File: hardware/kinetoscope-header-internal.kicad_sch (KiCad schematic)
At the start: 1 part

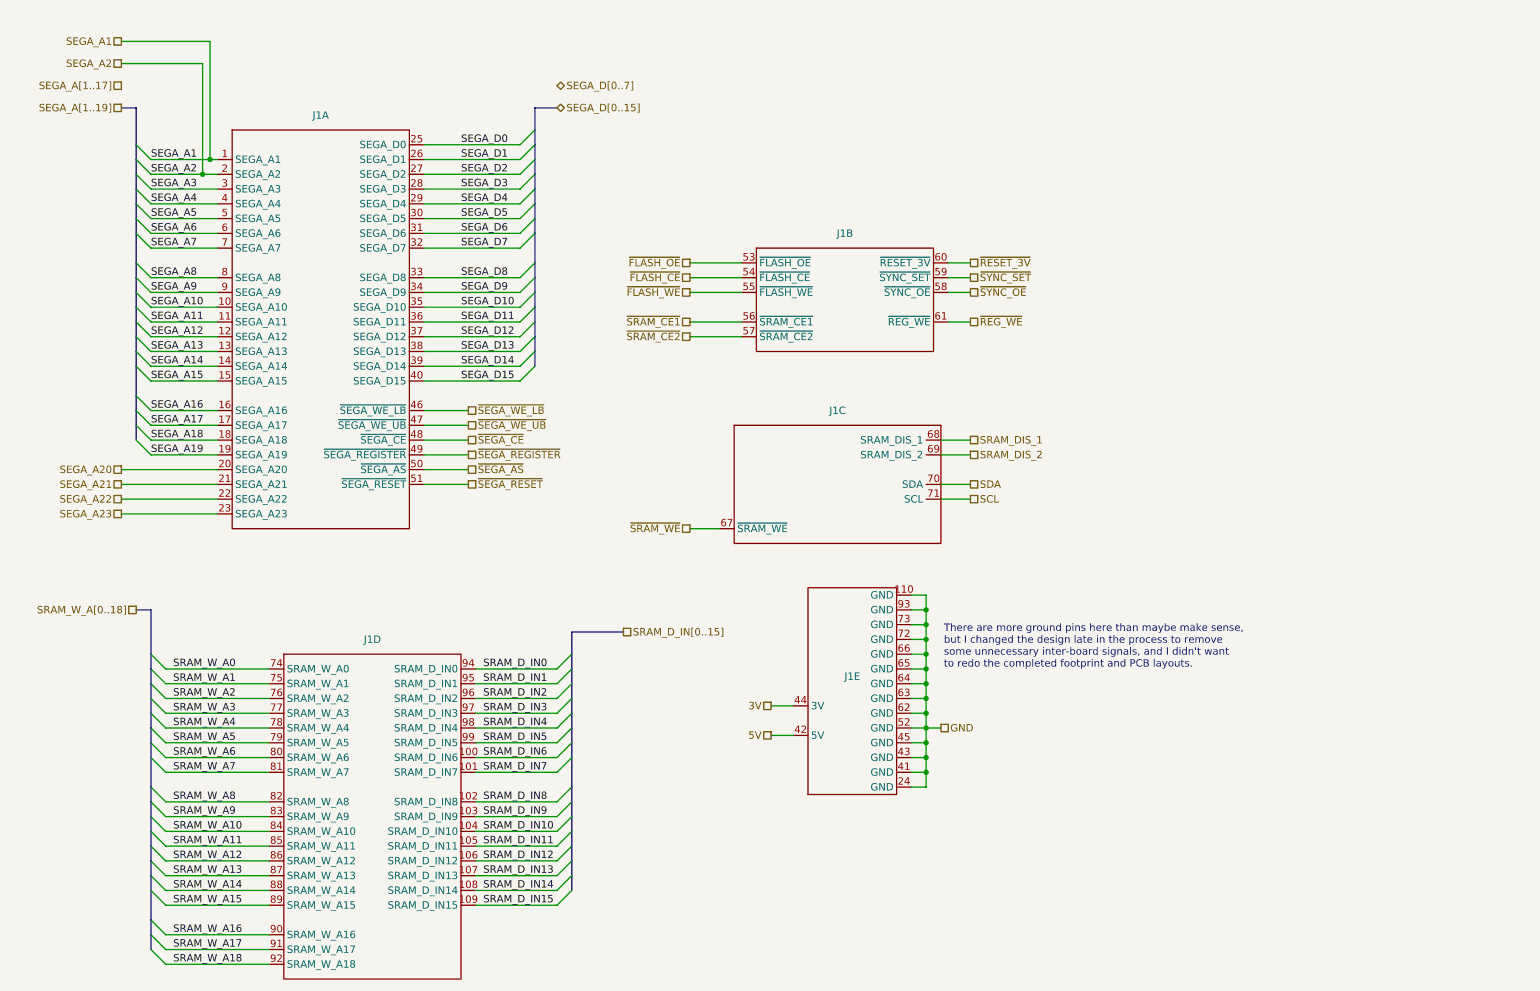
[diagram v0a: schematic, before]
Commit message: Massively reorganize board designs
Now planning to have most assembly done by JLCPCB, so trace sizes,
part selections, etc. are set accordingly.

New boards are:
 - cartridge interface & flash
 - microcontroller & registers
 - sram x2
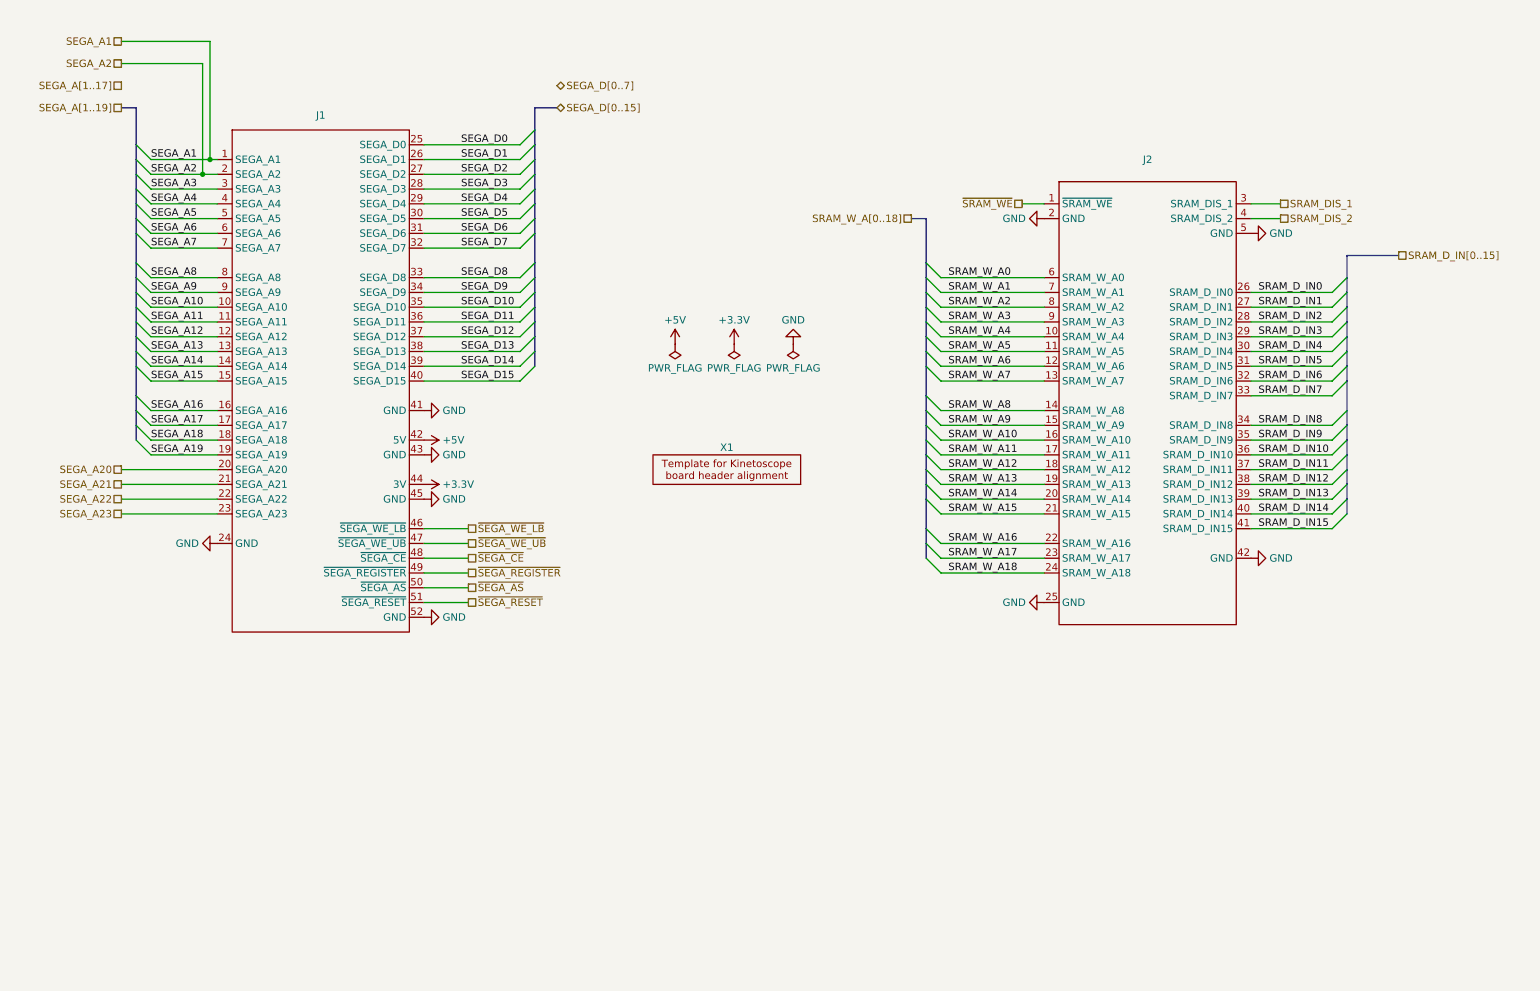
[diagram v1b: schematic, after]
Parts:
- removed J1: ~, kinetoscope-cart-header:kinetoscope-cart-header, symbol kinetoscope-cart-header:kinetoscope-cart-header
- added J1: ~, Connector_PinHeader_2.54mm:PinHeader_2x26_P2.54mm_Vertical, symbol kinetoscope-cart-header:kinetoscope-cart-header-a
- added J2: ~, Connector_PinHeader_2.54mm:PinHeader_2x21_P2.54mm_Vertical, symbol kinetoscope-cart-header:kinetoscope-cart-header-b
- added X1: ~, kinetoscope-cart-header:kinetoscope-cart-board-template, symbol kinetoscope-cart-header:kinetoscope-cart-template
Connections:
- net GND: now also J1.24 (GND), J1.41 (GND), J1.43 (GND), J1.45 (GND), J1.52 (GND), J2.2 (GND), J2.25 (GND), J2.42 (GND), J2.5 (GND)
- net SEGA_A1: now also J1.1 (SEGA_A1)
- net SEGA_A10: now also J1.10 (SEGA_A10)
- net SEGA_A11: now also J1.11 (SEGA_A11)
- net SEGA_A12: now also J1.12 (SEGA_A12)
- net SEGA_A13: now also J1.13 (SEGA_A13)
- net SEGA_A14: now also J1.14 (SEGA_A14)
- net SEGA_A15: now also J1.15 (SEGA_A15)
- net SEGA_A16: now also J1.16 (SEGA_A16)
- net SEGA_A17: now also J1.17 (SEGA_A17)
- net SEGA_A18: now also J1.18 (SEGA_A18)
- net SEGA_A19: now also J1.19 (SEGA_A19)
- net SEGA_A2: now also J1.2 (SEGA_A2)
- net SEGA_A20: now also J1.20 (SEGA_A20)
- net SEGA_A21: now also J1.21 (SEGA_A21)
- net SEGA_A22: now also J1.22 (SEGA_A22)
- net SEGA_A23: now also J1.23 (SEGA_A23)
- net SEGA_A3: now also J1.3 (SEGA_A3)
- net SEGA_A4: now also J1.4 (SEGA_A4)
- net SEGA_A5: now also J1.5 (SEGA_A5)
- net SEGA_A6: now also J1.6 (SEGA_A6)
- net SEGA_A7: now also J1.7 (SEGA_A7)
- net SEGA_A8: now also J1.8 (SEGA_A8)
- net SEGA_A9: now also J1.9 (SEGA_A9)
- net SEGA_D0: now also J1.25 (SEGA_D0)
- net SEGA_D1: now also J1.26 (SEGA_D1)
- net SEGA_D10: now also J1.35 (SEGA_D10)
- net SEGA_D11: now also J1.36 (SEGA_D11)
- net SEGA_D12: now also J1.37 (SEGA_D12)
- net SEGA_D13: now also J1.38 (SEGA_D13)
- net SEGA_D14: now also J1.39 (SEGA_D14)
- net SEGA_D15: now also J1.40 (SEGA_D15)
- net SEGA_D2: now also J1.27 (SEGA_D2)
- net SEGA_D3: now also J1.28 (SEGA_D3)
- net SEGA_D4: now also J1.29 (SEGA_D4)
- net SEGA_D5: now also J1.30 (SEGA_D5)
- net SEGA_D6: now also J1.31 (SEGA_D6)
- net SEGA_D7: now also J1.32 (SEGA_D7)
- net SEGA_D8: now also J1.33 (SEGA_D8)
- net SEGA_D9: now also J1.34 (SEGA_D9)
- net SRAM_DIS_1: now also J2.3 (SRAM_DIS_1)
- net SRAM_DIS_2: now also J2.4 (SRAM_DIS_2)
- net SRAM_D_IN0: now also J2.26 (SRAM_D_IN0)
- net SRAM_D_IN1: now also J2.27 (SRAM_D_IN1)
- net SRAM_D_IN10: now also J2.36 (SRAM_D_IN10)
- net SRAM_D_IN11: now also J2.37 (SRAM_D_IN11)
- net SRAM_D_IN12: now also J2.38 (SRAM_D_IN12)
- net SRAM_D_IN13: now also J2.39 (SRAM_D_IN13)
- net SRAM_D_IN14: now also J2.40 (SRAM_D_IN14)
- net SRAM_D_IN15: now also J2.41 (SRAM_D_IN15)
- net SRAM_D_IN2: now also J2.28 (SRAM_D_IN2)
- net SRAM_D_IN3: now also J2.29 (SRAM_D_IN3)
- net SRAM_D_IN4: now also J2.30 (SRAM_D_IN4)
- net SRAM_D_IN5: now also J2.31 (SRAM_D_IN5)
- net SRAM_D_IN6: now also J2.32 (SRAM_D_IN6)
- net SRAM_D_IN7: now also J2.33 (SRAM_D_IN7)
- net SRAM_D_IN8: now also J2.34 (SRAM_D_IN8)
- net SRAM_D_IN9: now also J2.35 (SRAM_D_IN9)
- net SRAM_W_A0: now also J2.6 (SRAM_W_A0)
- net SRAM_W_A1: now also J2.7 (SRAM_W_A1)
- net SRAM_W_A10: now also J2.16 (SRAM_W_A10)
- net SRAM_W_A11: now also J2.17 (SRAM_W_A11)
- net SRAM_W_A12: now also J2.18 (SRAM_W_A12)
- net SRAM_W_A13: now also J2.19 (SRAM_W_A13)
- net SRAM_W_A14: now also J2.20 (SRAM_W_A14)
- net SRAM_W_A15: now also J2.21 (SRAM_W_A15)
- net SRAM_W_A16: now also J2.22 (SRAM_W_A16)
- net SRAM_W_A17: now also J2.23 (SRAM_W_A17)
- net SRAM_W_A18: now also J2.24 (SRAM_W_A18)
- net SRAM_W_A2: now also J2.8 (SRAM_W_A2)
- net SRAM_W_A3: now also J2.9 (SRAM_W_A3)
- net SRAM_W_A4: now also J2.10 (SRAM_W_A4)
- net SRAM_W_A5: now also J2.11 (SRAM_W_A5)
- net SRAM_W_A6: now also J2.12 (SRAM_W_A6)
- net SRAM_W_A7: now also J2.13 (SRAM_W_A7)
- net SRAM_W_A8: now also J2.14 (SRAM_W_A8)
- net SRAM_W_A9: now also J2.15 (SRAM_W_A9)
- net ~{SEGA_AS}: now also J1.50 (~{SEGA_AS})
- net ~{SEGA_CE}: now also J1.48 (~{SEGA_CE})
- net ~{SEGA_REGISTER}: now also J1.49 (~{SEGA_REGISTER})
- net ~{SEGA_RESET}: now also J1.51 (~{SEGA_RESET})
- net ~{SEGA_WE_LB}: now also J1.46 (~{SEGA_WE_LB})
- net ~{SEGA_WE_UB}: now also J1.47 (~{SEGA_WE_UB})
- net ~{SRAM_WE}: now also J2.1 (~{SRAM_WE})
- new net +3.3V: J1.44 (3V)
- new net +5V: J1.42 (5V)
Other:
- note removed: "There are more ground pins here than maybe make sense, but I changed the design late in the process to remove some unnecessary inter-board signals, and I didn't want to redo the completed footprint and PCB layouts."

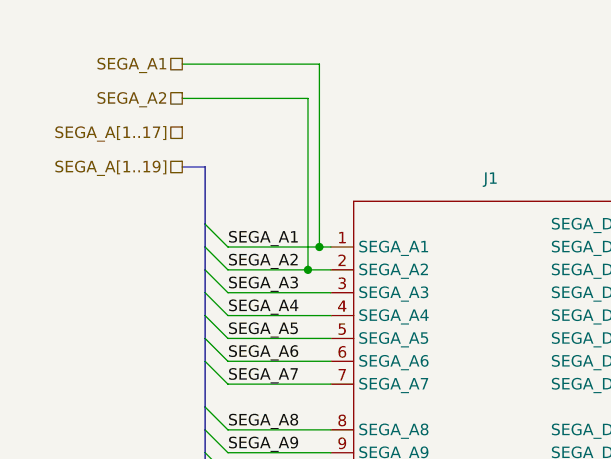
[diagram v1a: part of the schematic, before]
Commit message: Fix ethernet chip-select and register address decoder
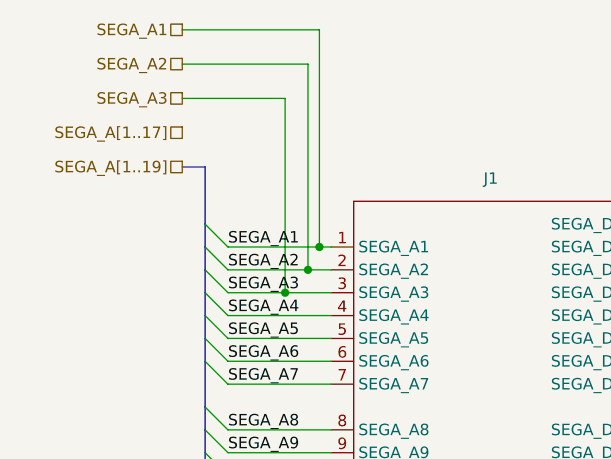
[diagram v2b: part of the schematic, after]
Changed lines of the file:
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@@
 		(color 0 0 0 0)
 	)
+	(junction
+		(at 39.37 44.45)
+		(diameter 0)
+		(color 0 0 0 0)
+	)
 	(bus_entry
 		(at 30.48 74.93)
@@
 	(wire
 		(pts
-			(xy 43.18 19.05) (xy 43.18 39.37)
+			(xy 43.18 15.24) (xy 43.18 39.37)
 		)
 		(stroke
@@
 		)
 	)
+	(wire
+		(pts
+			(xy 27.94 22.86) (xy 39.37 22.86)
+		)
+		(stroke
+			(width 0)
+			(type default)
+		)
+	)
 	(bus
 		(pts
@@
 	(wire
 		(pts
-			(xy 41.91 22.86) (xy 41.91 41.91)
+			(xy 41.91 19.05) (xy 41.91 41.91)
 		)
 		(stroke
@@
 	(wire
 		(pts
+			(xy 39.37 22.86) (xy 39.37 44.45)
+		)
+		(stroke
+			(width 0)
+			(type default)
+		)
+	)
+	(wire
+		(pts
 			(xy 80.01 46.99) (xy 96.52 46.99)
 		)
@@
 	(wire
 		(pts
-			(xy 33.02 44.45) (xy 44.45 44.45)
+			(xy 33.02 44.45) (xy 39.37 44.45)
 		)
 		(stroke
@@
 	(wire
 		(pts
-			(xy 27.94 19.05) (xy 43.18 19.05)
+			(xy 27.94 15.24) (xy 43.18 15.24)
 		)
 		(stroke
@@
 		)
 	)
+	(wire
+		(pts
+			(xy 39.37 44.45) (xy 44.45 44.45)
+		)
+		(stroke
+			(width 0)
+			(type default)
+		)
+	)
 	(bus
 		(pts
@@
 	(wire
 		(pts
-			(xy 27.94 22.86) (xy 41.91 22.86)
+			(xy 27.94 19.05) (xy 41.91 19.05)
 		)
 		(stroke
@@
 		)
 	)
+	(hierarchical_label "SEGA_A3"
+		(shape passive)
+		(at 27.94 22.86 180)
+		(fields_autoplaced yes)
+		(effects
+			(font
+				(size 1.27 1.27)
+			)
+			(justify right)
+		)
+	)
 	(hierarchical_label "~{SEGA_REGISTER}"
 		(shape passive)
@@
 	(hierarchical_label "SEGA_A2"
 		(shape passive)
-		(at 27.94 22.86 180)
+		(at 27.94 19.05 180)
 		(fields_autoplaced yes)
 		(effects
@@
 	(hierarchical_label "SEGA_A1"
 		(shape passive)
-		(at 27.94 19.05 180)
-		(fields_autoplaced yes)
-		(effects
+		(at 27.94 15.24 180)
+		(fields_autoplaced yes)
+		(effects

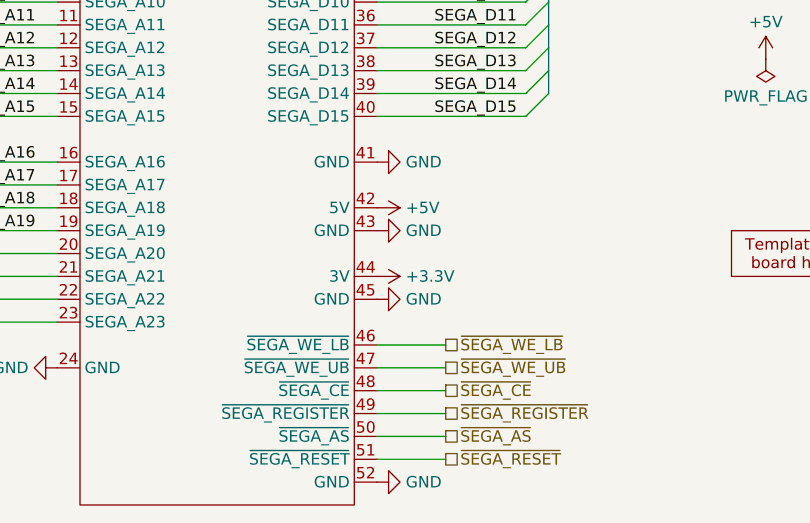
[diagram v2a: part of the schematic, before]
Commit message: Update interboard header in microcontroller and SRAM boards
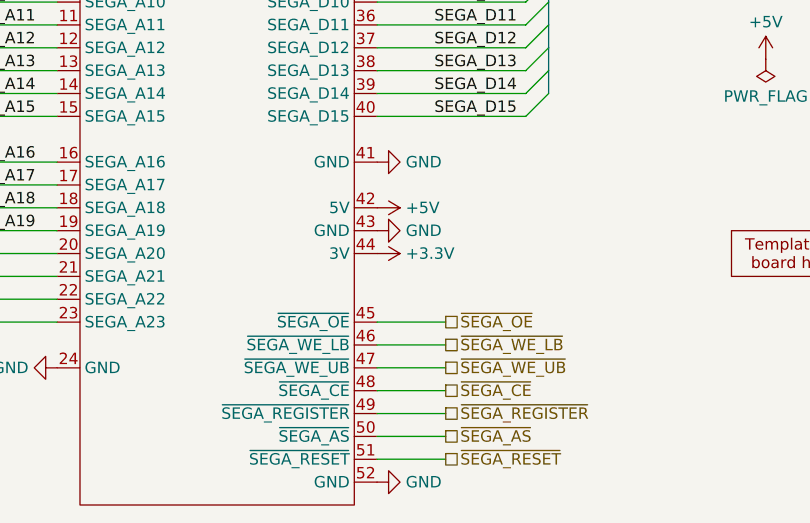
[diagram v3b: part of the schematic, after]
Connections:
- net GND: no longer J1.45 (GND)
- new net ~{SEGA_OE}: J1.45 (~{SEGA_OE})
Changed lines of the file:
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@@
 	(wire
 		(pts
+			(xy 80.01 100.33) (xy 87.63 100.33)
+		)
+		(stroke
+			(width 0)
+			(type default)
+		)
+	)
+	(wire
+		(pts
 			(xy 222.25 64.77) (xy 236.22 64.77)
 		)
@@
 		)
 	)
+	(hierarchical_label "~{SEGA_OE}"
+		(shape passive)
+		(at 87.63 100.33 0)
+		(fields_autoplaced yes)
+		(effects
+			(font
+				(size 1.27 1.27)
+			)
+			(justify left)
+		)
+	)
 	(hierarchical_label "SEGA_A2"
 		(shape passive)
@@
 	(symbol
 		(lib_id "power:GND")
-		(at 80.01 97.79 90)
-		(unit 1)
-		(exclude_from_sim no)
-		(in_bom yes)
-		(on_board yes)
-		(dnp no)
-		(fields_autoplaced yes)
-		(property "Reference" "#PWR03"
-			(at 86.36 97.79 0)
-			(effects
-				(font
-					(size 1.27 1.27)
-				)
-				(hide yes)
-			)
-		)
-		(property "Value" "GND"
-			(at 83.185 97.79 90)
-			(effects
-				(font
-					(size 1.27 1.27)
-				)
-				(justify right)
-			)
-		)
-		(property "Footprint" ""
-			(at 80.01 97.79 0)
-			(effects
-				(font
-					(size 1.27 1.27)
-				)
-				(hide yes)
-			)
-		)
-		(property "Datasheet" ""
-			(at 80.01 97.79 0)
-			(effects
-				(font
-					(size 1.27 1.27)
-				)
-				(hide yes)
-			)
-		)
-		(property "Description" "Power symbol creates a global label with name \"GND\" , ground"
-			(at 80.01 97.79 0)
-			(effects
-				(font
-					(size 1.27 1.27)
-				)
-				(hide yes)
-			)
-		)
-		(pin "1"
-		)
-		(instances
-			(project "microcontroller"
-				(path "/eb0e957f-b2ea-4261-97c1-e28148a3f6e1/3a2d4409-520b-42a9-988d-13f6351a40c4"
-					(reference "#PWR03")
-					(unit 1)
-				)
-			)
-		)
-	)
-	(symbol
-		(lib_id "power:GND")
 		(at 186.69 49.53 270)
 		(unit 1)
@@
 	(symbol
 		(lib_id "power:+3.3V")
-		(at 80.01 95.25 270)
+		(at 80.01 92.71 270)
 		(unit 1)
 		(exclude_from_sim no)
@@
 		(fields_autoplaced yes)
 		(property "Reference" "#PWR011"
-			(at 76.2 95.25 0)
+			(at 76.2 92.71 0)
 			(effects
 				(font
@@
 		)
 		(property "Value" "+3.3V"
-			(at 83.185 95.25 90)
+			(at 83.185 92.71 90)
 			(effects
 				(font
@@
 		)
 		(property "Footprint" ""
-			(at 80.01 95.25 0)
+			(at 80.01 92.71 0)
 			(effects
 				(font
@@
 		)
 		(property "Datasheet" ""
-			(at 80.01 95.25 0)
+			(at 80.01 92.71 0)
 			(effects
 				(font
@@
 		)
 		(property "Description" "Power symbol creates a global label with name \"+3.3V\""
-			(at 80.01 95.25 0)
+			(at 80.01 92.71 0)
 			(effects
 				(font

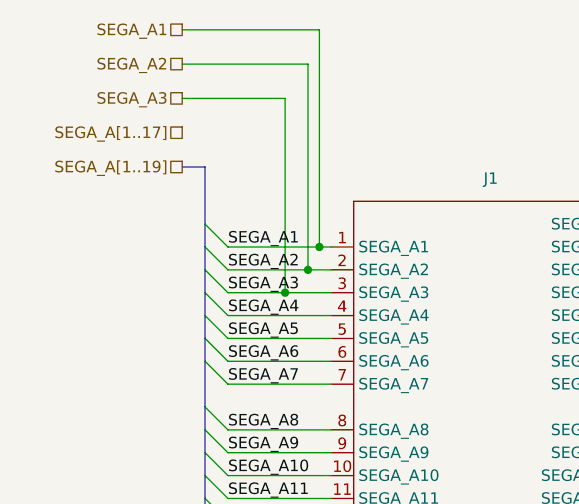
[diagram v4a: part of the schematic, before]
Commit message: Improve uC board assembly further
Change the register file CD74HC670M96 with SN74AHC373PWR and an
inverter, which is more easily available from JLCPCB.

This is not an exact replacement, as we replaced 2x 4x4 register files
with 2x 8-bit latches.  So instead of 4x 8-bit registers, we now only
have 2x 8-bit registers, but we only used 2 to begin with.

The new register hardware required us to change the address decoding
and the actual addresses of the registers.  Instead of 0xA13000 and
0xA13002, we now write to 0xA13010 and 0xA13012.
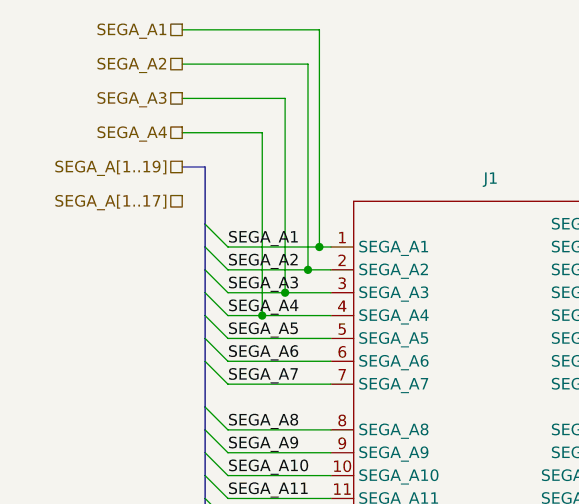
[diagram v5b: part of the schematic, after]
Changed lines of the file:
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@@
 		(color 0 0 0 0)
 	)
+	(junction
+		(at 36.83 46.99)
+		(diameter 0)
+		(color 0 0 0 0)
+	)
 	(bus_entry
 		(at 30.48 74.93)
@@
 		)
 	)
+	(wire
+		(pts
+			(xy 36.83 46.99) (xy 44.45 46.99)
+		)
+		(stroke
+			(width 0)
+			(type default)
+		)
+	)
 	(bus
 		(pts
@@
 		)
 	)
+	(wire
+		(pts
+			(xy 36.83 26.67) (xy 36.83 46.99)
+		)
+		(stroke
+			(width 0)
+			(type default)
+		)
+	)
 	(bus
 		(pts
@@
 	(wire
 		(pts
-			(xy 33.02 46.99) (xy 44.45 46.99)
+			(xy 27.94 26.67) (xy 36.83 26.67)
+		)
+		(stroke
+			(width 0)
+			(type default)
+		)
+	)
+	(wire
+		(pts
+			(xy 33.02 46.99) (xy 36.83 46.99)
 		)
 		(stroke
@@
 	(hierarchical_label "SEGA_A[1..17]"
 		(shape passive)
-		(at 27.94 26.67 180)
+		(at 27.94 34.29 180)
 		(fields_autoplaced yes)
 		(effects
@@
 		(fields_autoplaced yes)
 		(effects
+			(font
+				(size 1.27 1.27)
+			)
+			(justify right)
+		)
+	)
+	(hierarchical_label "SEGA_A4"
+		(shape passive)
+		(at 27.94 26.67 180)
+		(fields_autoplaced yes)
+		(effects

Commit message: Add part numbers for all headers
You can still choose to leave these off of an assembly order and populate them yourself.
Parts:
- J1: JLCPCB Part Number (none) -> C3323945; Mouser Part Number (none) -> 200-SSW12602TD; Part Number (none) -> SSW-126-02-T-D
- J2: JLCPCB Part Number (none) -> C3324002; Mouser Part Number (none) -> 200-SSW12102TD; Part Number (none) -> SSW-121-02-T-D
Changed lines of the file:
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@@
 			)
 		)
-		(property "JLCPCB Part Number" ""
+		(property "JLCPCB Part Number" "C3324002"
+			(at 204.47 41.91 0)
+			(effects
+				(font
+					(size 1.27 1.27)
+				)
+				(hide yes)
+			)
+		)
+		(property "Mouser Part Number" "200-SSW12102TD"
+			(at 204.47 41.91 0)
+			(effects
+				(font
+					(size 1.27 1.27)
+				)
+				(hide yes)
+			)
+		)
+		(property "Part Number" "SSW-121-02-T-D"
 			(at 204.47 41.91 0)
 			(effects
@@
 			)
 		)
-		(property "JLCPCB Part Number" ""
+		(property "JLCPCB Part Number" "C3323945"
 			(at 62.23 34.29 0)
 			(effects
@@
 			)
 		)
-		(property "Mouser Part Number" ""
+		(property "Mouser Part Number" "200-SSW12602TD"
 			(at 62.23 34.29 0)
 			(effects
@@
 			)
 		)
-		(property "Part Number" ""
+		(property "Part Number" "SSW-126-02-T-D"
 			(at 62.23 34.29 0)
 			(effects
